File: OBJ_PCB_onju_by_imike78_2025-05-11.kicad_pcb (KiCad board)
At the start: 4 copper layers, 74.5 x 70.6 mm, 179 parts, among them J1 1775443-2, J2 usb_c, Q1 LBSS138WT1G, Q2 BC847B, SW1 CHS-01TA, U1 TPS62130, U10 SN74LVC125APWR, U11 MAX98357AETE_T, U12 FSUSB42MUX, U13 AP22802AW5-7, U2 MIC5365-1.8YC5-TR, U3 TPS62130, U4 MIC5365-0.9YC5-TR, U5 ESP32-S3R8, U6 W25Q128JVSIQ, U7 XU316-1024-QF60B-C24, U8 W25Q128JVSIQ, U9 TLV73333PDBVR, Y1 40MHz, Y2 24MHz

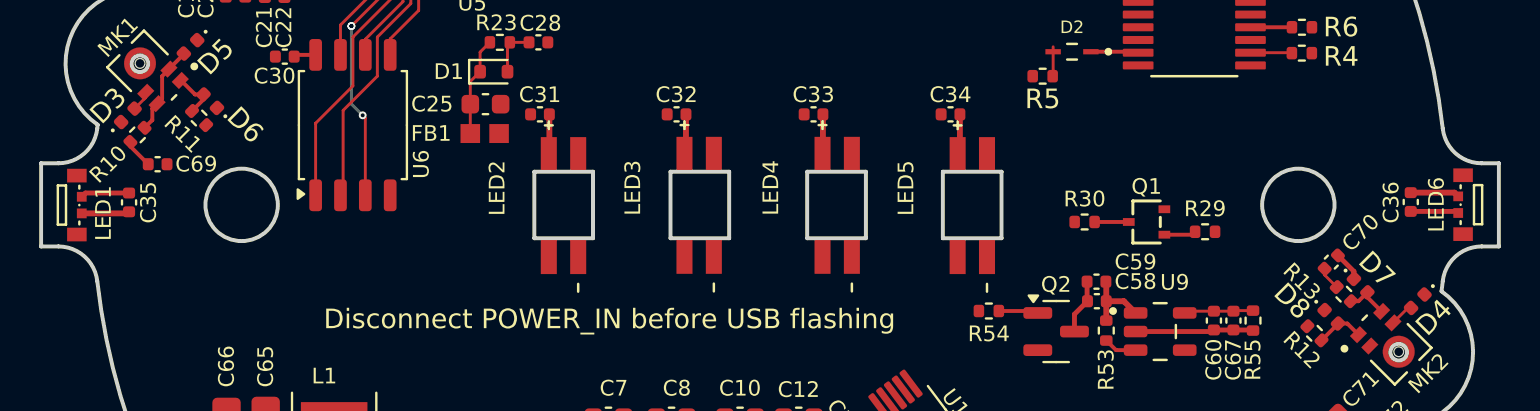
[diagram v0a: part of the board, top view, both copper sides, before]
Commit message: Route LED connections
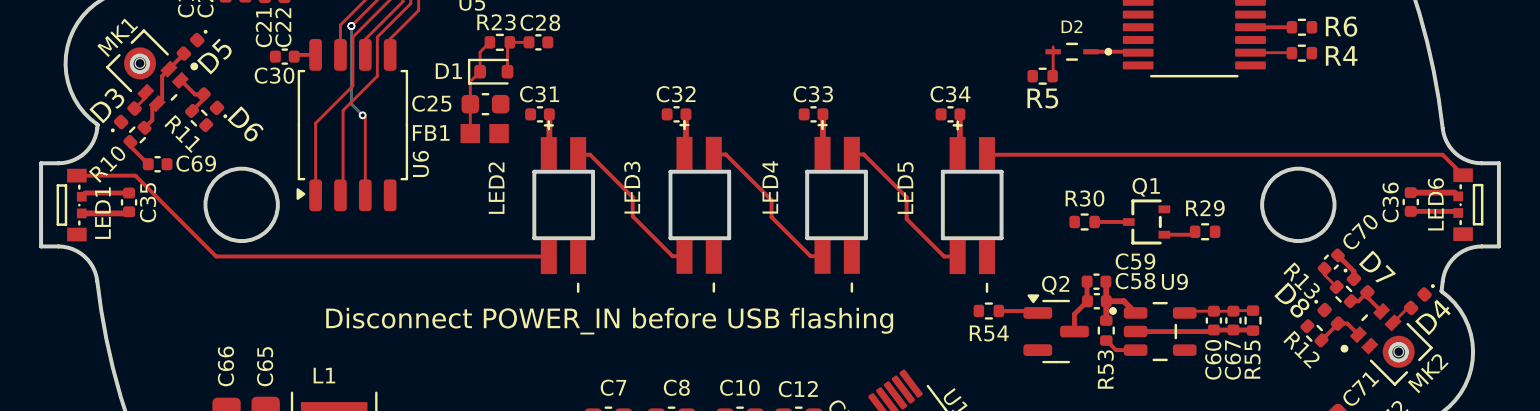
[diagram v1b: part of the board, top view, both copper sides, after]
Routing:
- net Net-(LED1-DOUT): track 0.00 -> 25.8 mm
- net Net-(LED5-DOUT): track 0.00 -> 24.8 mm
- net Net-(LED3-DOUT): track 0.00 -> 8.22 mm
- net Net-(LED4-DOUT): track 0.00 -> 8.21 mm
- net Net-(LED2-DOUT): track 0.00 -> 8.15 mm
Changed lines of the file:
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@@
+	)
+	(segment
+		(start 100.39519 87.581878)
+		(end 103.381878 87.581878)
+		(width 0.2)
+		(layer "F.Cu")
+		(net 80)
+	)
+	(segment
+		(start 103.381878 87.581878)
+		(end 107.513546 91.713546)
+		(width 0.2)
+		(layer "F.Cu")
+		(net 80)
+	)
+	(segment
+		(start 107.513546 91.713546)
+		(end 124.512358 91.713546)
+		(width 0.2)
+		(layer "F.Cu")
+		(net 80)
+	)
+	(segment
+		(start 128.8 88.691188)
+		(end 126.622358 86.513546)
+		(width 0.2)
+		(layer "F.Cu")
+		(net 81)
+	)
+	(segment
+		(start 126.622358 86.513546)
+		(end 126.012358 86.513546)
+		(width 0.2)
+		(layer "F.Cu")
+		(net 81)
+	)
+	(segment
+		(start 131.445818 91.7)
+		(end 130.835818 91.7)
+		(width 0.2)
+		(layer "F.Cu")
+		(net 81)
+	)
+	(segment
+		(start 130.835818 91.7)
+		(end 128.8 89.664182)
+		(width 0.2)
+		(layer "F.Cu")
+		(net 81)
+	)
+	(segment
+		(start 128.8 89.664182)
+		(end 128.8 88.691188)
+		(width 0.2)
+		(layer "F.Cu")
+		(net 81)
+	)
+	(segment
+		(start 137.89 91.7)
+		(end 135.895 89.705)
+		(width 0.2)
+		(layer "F.Cu")
+		(net 82)
+	)
+	(segment
+		(start 133.555818 86.5)
+		(end 132.945818 86.5)
+		(width 0.2)
+		(layer "F.Cu")
+		(net 82)
+	)
+	(segment
+		(start 138.5 91.7)
+		(end 137.89 91.7)
+		(width 0.2)
+		(layer "F.Cu")
+		(net 82)
+	)
+	(segment
+		(start 135.895 88.839182)
+		(end 133.555818 86.5)
+		(width 0.2)
+		(layer "F.Cu")
+		(net 82)
+	)
+	(segment
+		(start 135.895 89.705)
+		(end 135.895 88.839182)
+		(width 0.2)
+		(layer "F.Cu")
+		(net 82)
+	)
+	(segment
+		(start 142.8 88.69)
+		(end 140.61 86.5)
+		(width 0.2)
+		(layer "F.Cu")
+		(net 83)
+	)
+	(segment
+		(start 145.405181 91.713546)
+		(end 144.713546 91.713546)
+		(width 0.2)
+		(layer "F.Cu")
+		(net 83)
+	)
+	(segment
+		(start 140.61 86.5)
+		(end 140 86.5)
+		(width 0.2)
+		(layer "F.Cu")
+		(net 83)
+	)
+	(segment
+		(start 144.713546 91.713546)
+		(end 142.8 89.8)
+		(width 0.2)
+		(layer "F.Cu")
+		(net 83)
+	)
+	(segment
+		(start 142.8 89.8)
+		(end 142.8 88.69)
+		(width 0.2)
+		(layer "F.Cu")
+		(net 83)
+	)
+	(segment
+		(start 146.905181 86.513546)
+		(end 170.186641 86.513546)
+		(width 0.2)
+		(layer "F.Cu")
+		(net 84)
+	)
+	(segment
+		(start 170.186641 86.513546)
+		(end 171.234987 87.561892)
+		(width 0.2)
+		(layer "F.Cu")
+		(net 84)
 	)
 	(segment

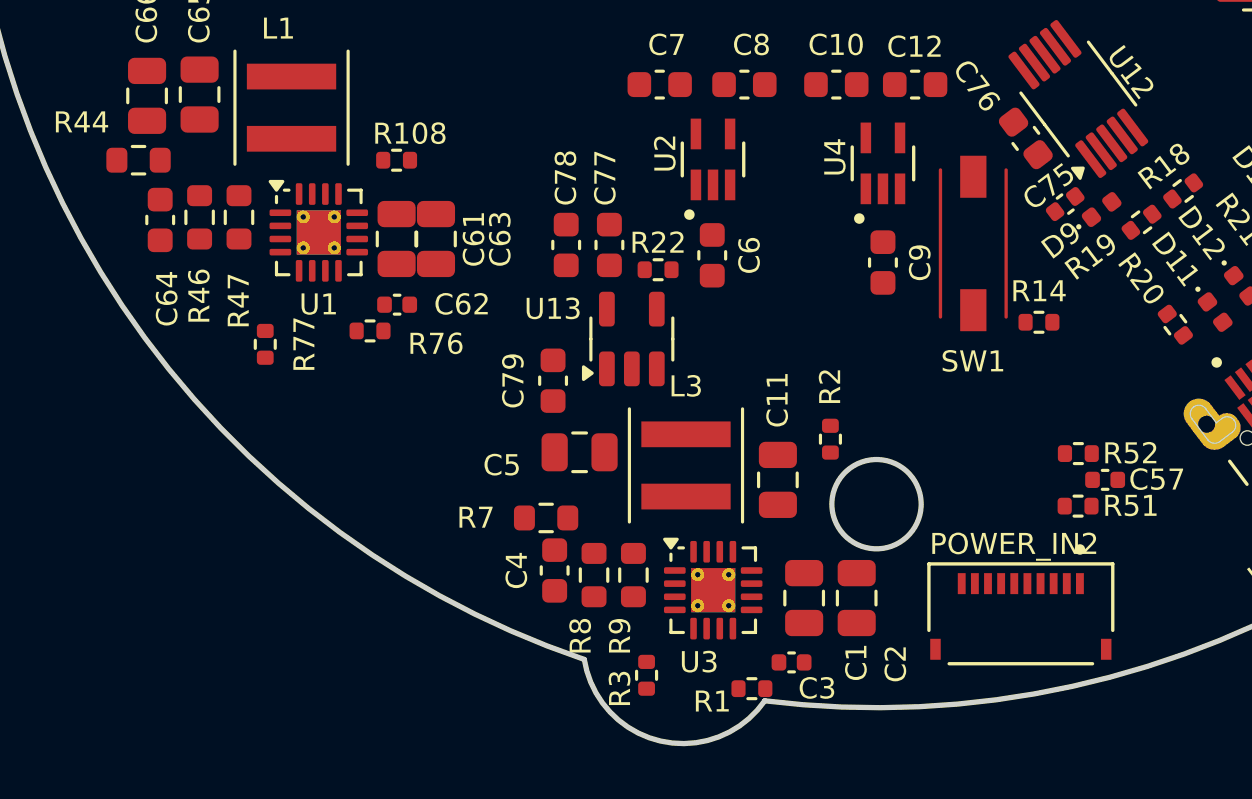
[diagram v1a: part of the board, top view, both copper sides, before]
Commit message: Route a few more miscellancous connections
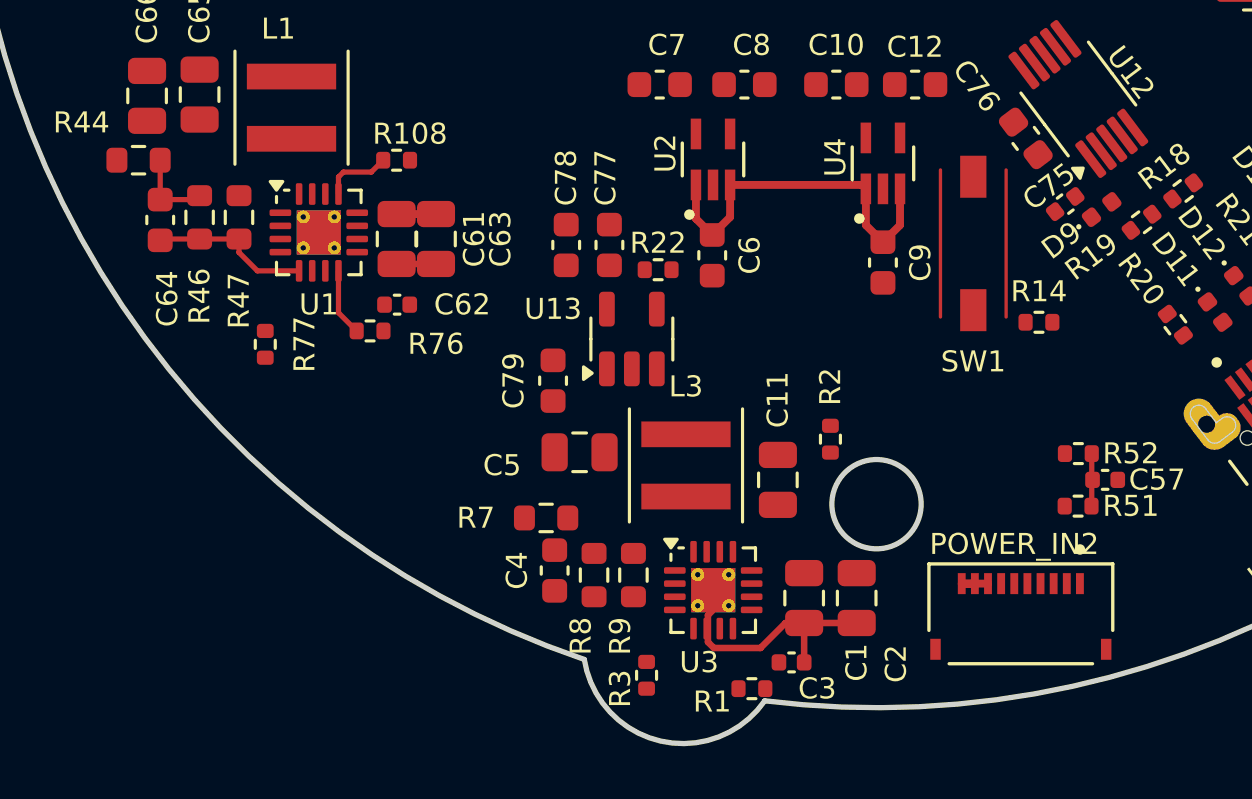
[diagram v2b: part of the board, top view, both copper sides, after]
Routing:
- net +3V3: track 0.00 -> 14.2 mm
- net GND: track 44.9 -> 56.0 mm
- net Net-(U1-FB): track 0.00 -> 6.11 mm
- net Net-(C64-Pad1): track 0.00 -> 3.06 mm
- net Net-(U1-EN): track 0.00 -> 2.62 mm
- net Net-(U1-DEF): track 0.00 -> 2.57 mm
- net MUTE_ON: track 0.00 -> 2.00 mm
- net +5V: track 19.4 -> 20.9 mm
- net +14V: track 0.00 -> 1.50 mm

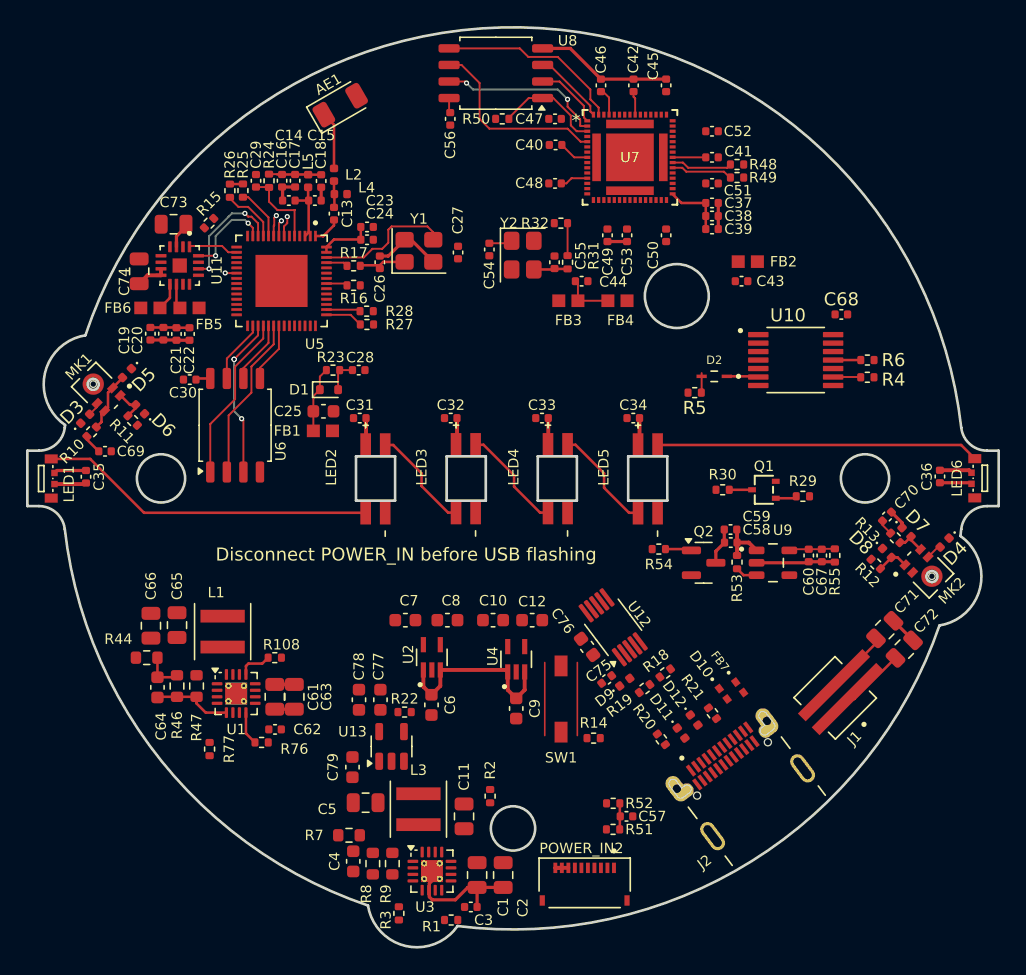
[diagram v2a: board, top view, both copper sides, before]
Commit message: Route a new more miscellaneous connections
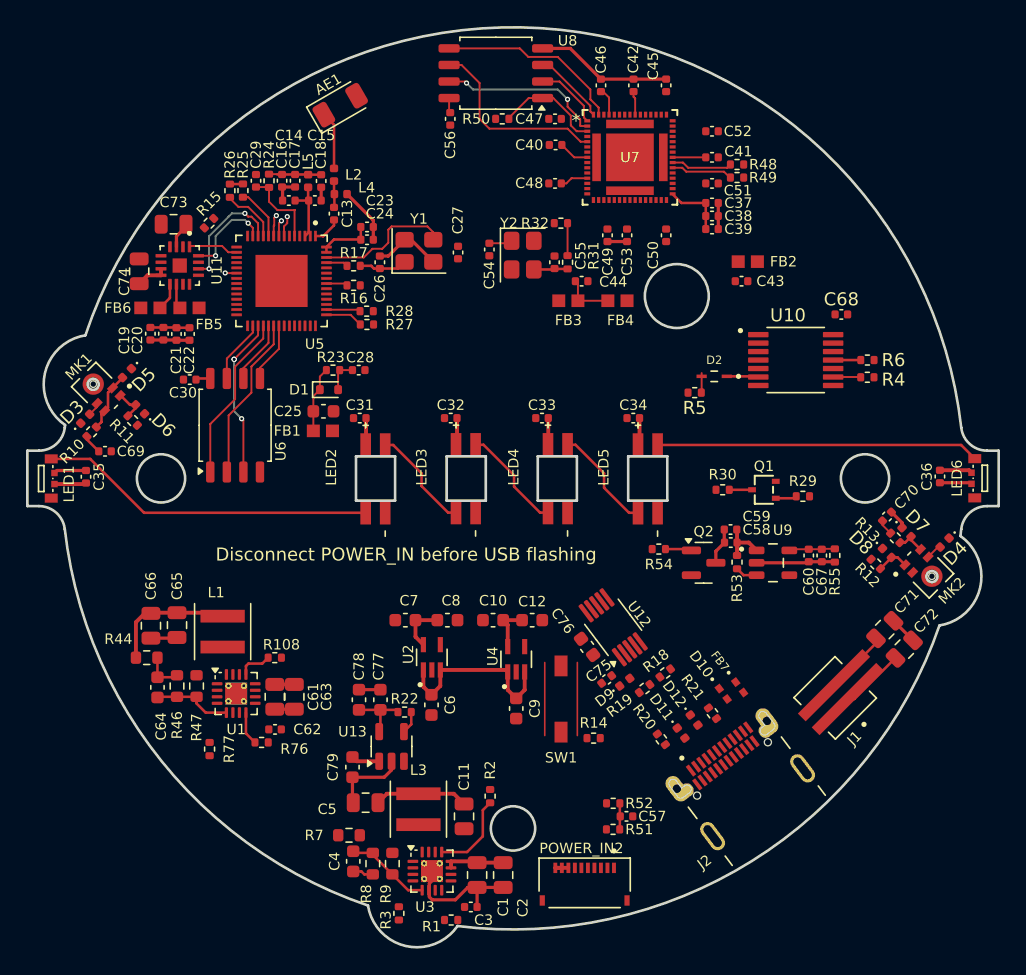
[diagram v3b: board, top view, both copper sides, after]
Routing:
- net GND: track 56.0 -> 70.1 mm
- net +3V3: track 14.2 -> 24.0 mm
- net +5V: track 20.9 -> 30.3 mm
- net Net-(U3-FB): track 0.00 -> 6.61 mm
- net Net-(U3-EN): track 0.00 -> 6.45 mm
- net VBUS: track 1.63 -> 6.40 mm
- net +14V: track 1.50 -> 6.04 mm
- net +1V8: track 4.82 -> 8.62 mm
- net +0V9: track 0.00 -> 3.62 mm
- net Net-(U13-EN): track 0.00 -> 1.73 mm
- net Net-(C4-Pad1): track 0.00 -> 1.59 mm
